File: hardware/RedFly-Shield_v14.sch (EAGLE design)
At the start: 66 parts, among them IC1 74LVC244, U1 TS1117-3.3V, X1 PASSER, X2 PASSER, X3 PASSER, X4 PASSER

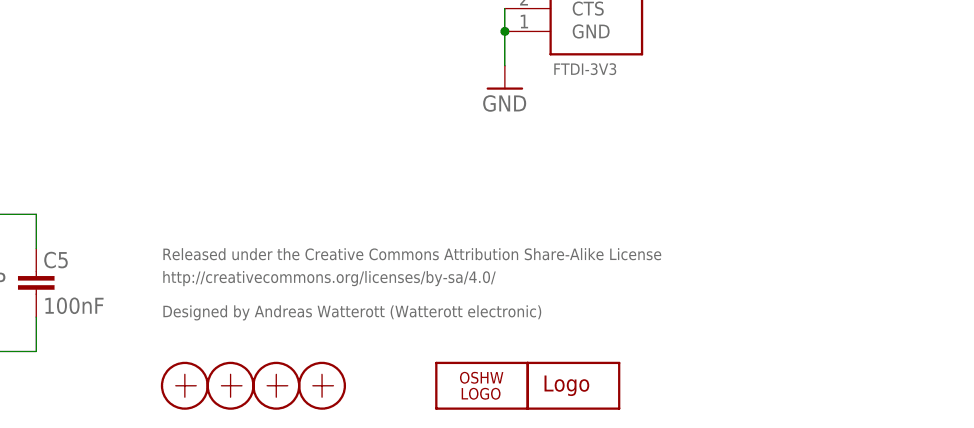
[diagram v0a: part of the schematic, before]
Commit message: updated schematics
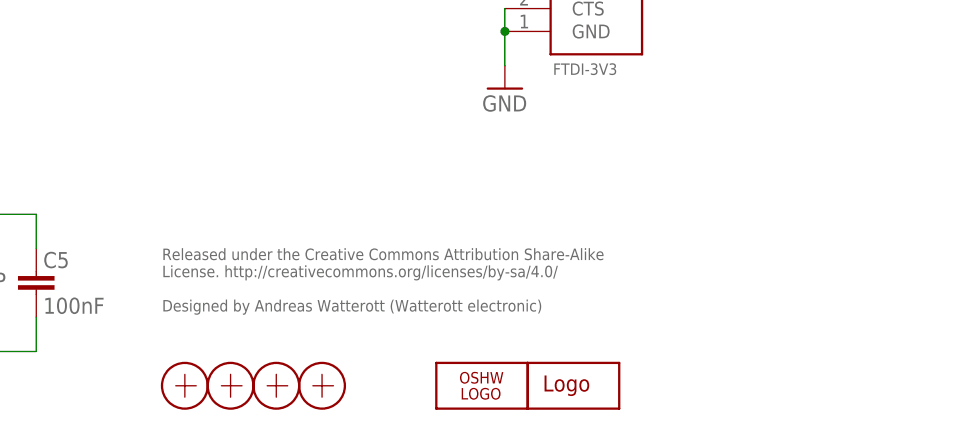
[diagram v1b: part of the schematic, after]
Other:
- note added: "Released under the Creative Commons Attribution Share-Alike License. http://creativecommons.org/licenses/by-sa/4.0/ Designed by Andreas Watterott (Watterott electronic)"
- note removed: "Designed by Andreas Watterott (Watterott electronic)"
- note removed: "Released under the Creative Commons Attribution Share-Alike License"
- note removed: "http://creativecommons.org/licenses/by-sa/4.0/"
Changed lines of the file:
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@@
 <?xml version="1.0" encoding="utf-8"?>
 <!DOCTYPE eagle SYSTEM "eagle.dtd">
-<eagle version="6.6.0">
+<eagle version="7.5.0">
 <drawing>
 <settings>
@@
 <layer number="51" name="tDocu" color="7" fill="1" visible="no" active="no"/>
 <layer number="52" name="bDocu" color="7" fill="1" visible="no" active="no"/>
-<layer number="53" name="tCopper" color="7" fill="11" visible="no" active="no"/>
-<layer number="54" name="bCopper" color="7" fill="1" visible="no" active="no"/>
-<layer number="56" name="wert" color="7" fill="1" visible="no" active="no"/>
 <layer number="91" name="Nets" color="2" fill="1" visible="yes" active="yes"/>
 <layer number="92" name="Busses" color="1" fill="1" visible="yes" active="yes"/>
@@
 <layer number="97" name="Info" color="7" fill="1" visible="yes" active="yes"/>
 <layer number="98" name="Guide" color="6" fill="1" visible="yes" active="yes"/>
-<layer number="100" name="Muster" color="7" fill="1" visible="no" active="no"/>
-<layer number="250" name="Descript" color="3" fill="1" visible="yes" active="yes"/>
-<layer number="251" name="SMDround" color="12" fill="11" visible="no" active="no"/>
 </layers>
 <schematic xreflabel="%F%N/%S.%C%R" xrefpart="/%S.%C%R">
@@
 <wire x1="72.39" y1="71.12" x2="75.057" y2="71.12" width="0.8128" layer="94"/>
 <wire x1="114.3" y1="71.12" x2="116.967" y2="71.12" width="0.8128" layer="94"/>
-<text x="162.56" y="21.59" size="1.27" layer="95">Released under the Creative Commons Attribution Share-Alike License</text>
-<text x="162.56" y="19.05" size="1.27" layer="95">http://creativecommons.org/licenses/by-sa/4.0/</text>
-<text x="162.56" y="15.24" size="1.27" layer="95">Designed by Andreas Watterott (Watterott electronic)</text>
+<text x="162.56" y="22.86" size="1.27" layer="95" align="top-left">Released under the Creative Commons Attribution Share-Alike
+License. http://creativecommons.org/licenses/by-sa/4.0/
+Designed by Andreas Watterott (Watterott electronic)</text>
 <text x="52.07" y="166.37" size="3.81" layer="250">Arduino</text>
 <text x="46.99" y="74.93" size="3.81" layer="250">Level Converter</text>
@@
 </schematic>
 </drawing>
+<compatibility>
+<note version="6.3" minversion="6.2.2" severity="warning">
+Since Version 6.2.2 text objects can contain more than one line,
+which will not be processed correctly with this version.
+</note>
+</compatibility>
 </eagle>
